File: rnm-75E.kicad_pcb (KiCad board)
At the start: 2 copper layers, 323.8 x 114.3 mm, 217 parts, among them J1 AVR-ISP-6, J2 USB_C_Receptacle_USB2.0, J3 Conn_01x04, SW1 SW_Push, SW2 Rotary_Encoder_Switch, U1 AT90USB646-AU, Y1 Crystal_GND24_Small

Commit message: WIRED SPI
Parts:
- C_ucap1, SW1: moved to B.Cu
- moved J1 311.5 mm to (646.9, -4.76)
- moved C_ucap1 168.3 mm to (523.1, 64.3), turned to 180 degrees
- moved SW1 125.0 mm to (585.7, 67.7), turned to 0 degrees
- moved R1 6.74 mm to (648.5, -20.8)
- moved CF3 6.70 mm to (530.4, 69.1), turned to 0 degrees
- moved D57 5.02 mm to (537.4, 55.6), turned to 270 degrees
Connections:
- U1 pad 10: LED_PIN -> LED
- U1 pad 9: LED -> LED_PIN
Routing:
- net LED_PIN: track 31.0 -> 263.2 mm, vias 0 -> 1
- net MOSI: track 0.00 -> 204.9 mm
- net GND: track 36.3 -> 237.6 mm
- net MISO: track 0.00 -> 185.3 mm, vias 0 -> 2
- net SCK: track 0.00 -> 183.9 mm
- net RESET: track 0.00 -> 70.9 mm
- net Net-(C_ucap1-Pad2): track 0.00 -> 17.4 mm
- net +5V: track 233.0 -> 249.0 mm, vias 0 -> 2
- net Net-(CAPS_LOCK_LED1-Pad1): track 23.6 -> 28.4 mm
- net Net-(D57-Pad2): track 6.82 -> 4.62 mm
- net ROWE: track 0.00 -> 0.67 mm

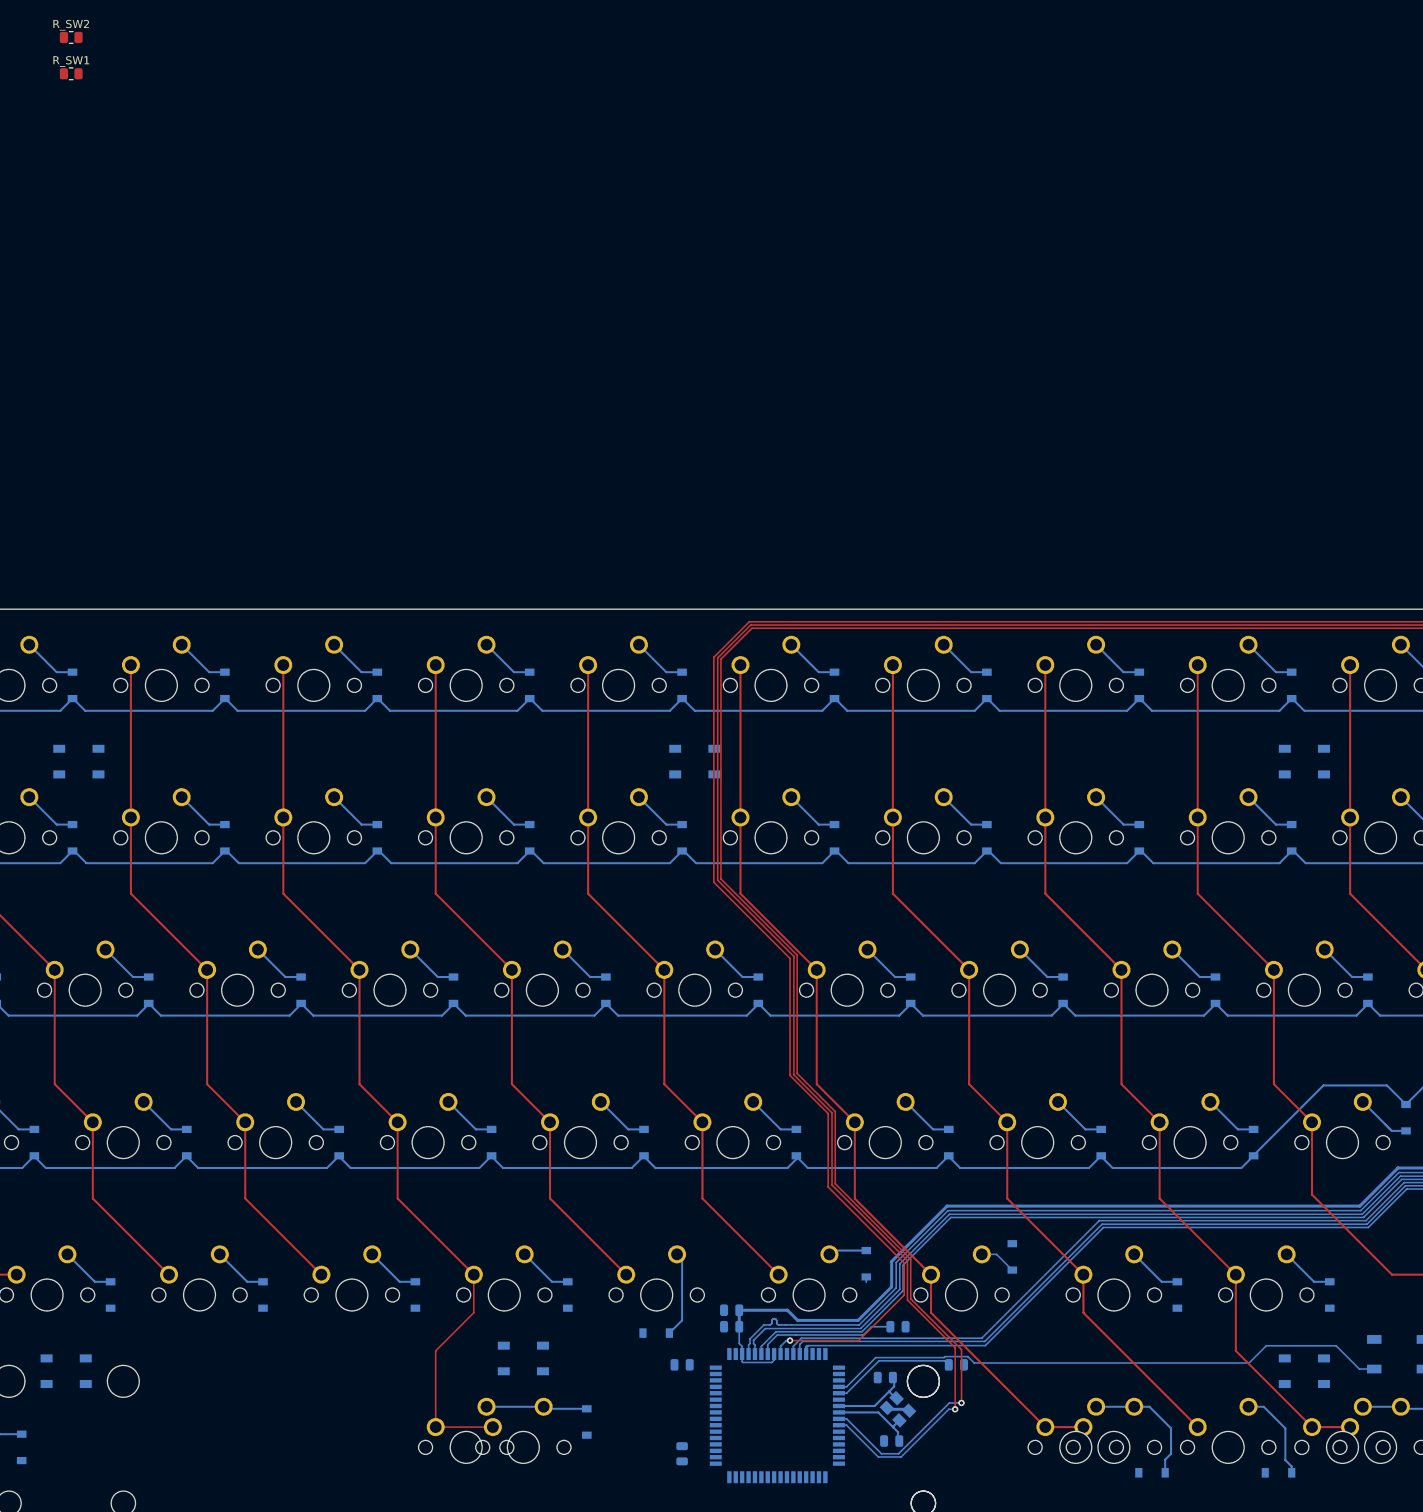
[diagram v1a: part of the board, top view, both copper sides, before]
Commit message: move sw res
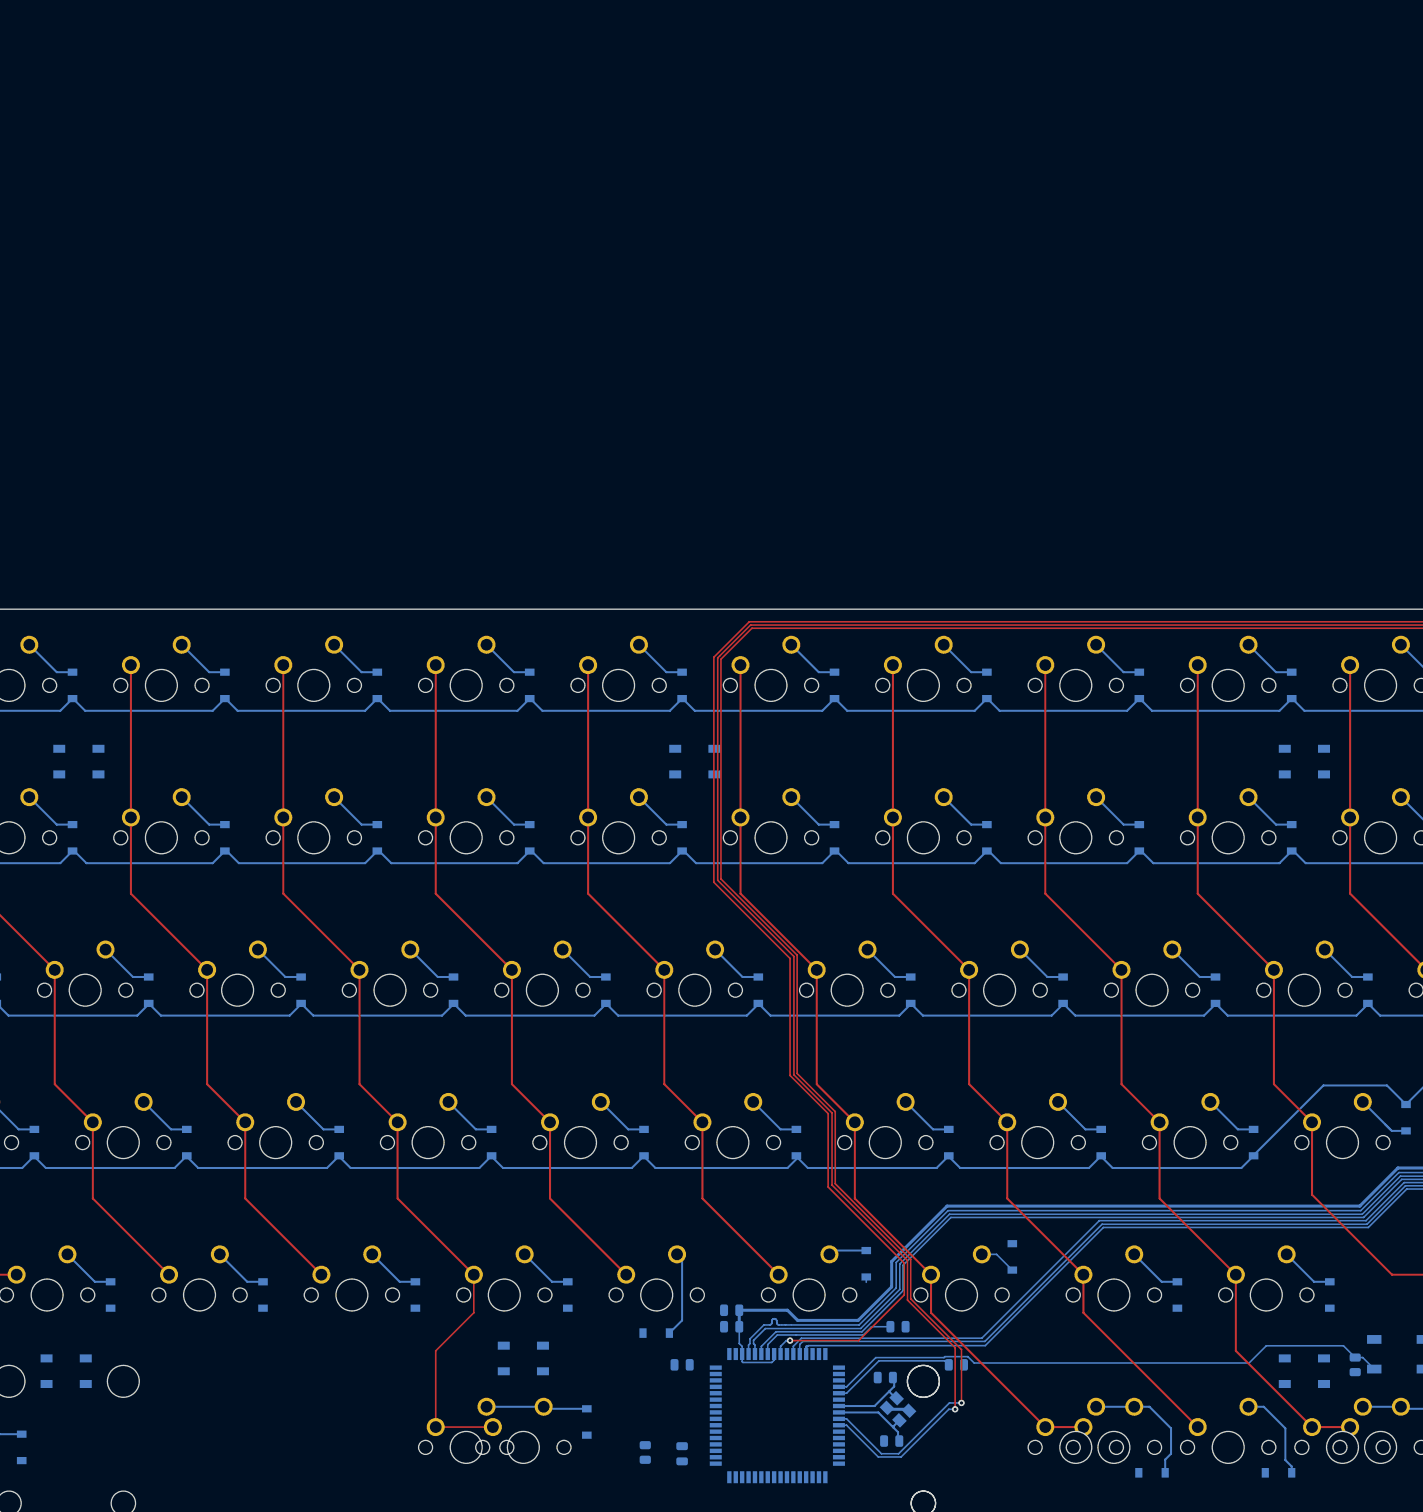
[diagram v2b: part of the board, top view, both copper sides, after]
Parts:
- R_SW1, R_SW2: moved to B.Cu
- moved R_SW1 227.6 mm to (580.2, 69.1), turned to 270 degrees
- moved R_SW2 190.9 mm to (491.5, 80.0), turned to 90 degrees

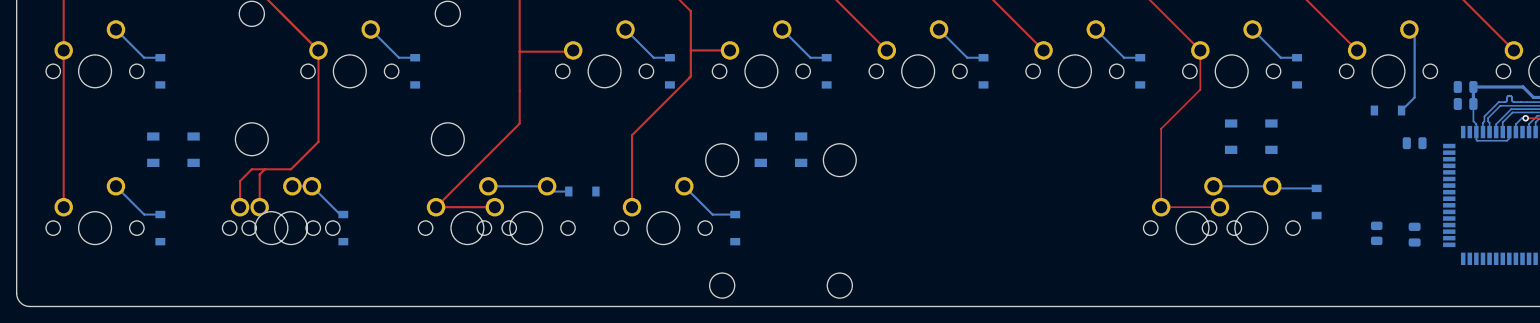
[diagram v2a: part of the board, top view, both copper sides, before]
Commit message: route column 1-6
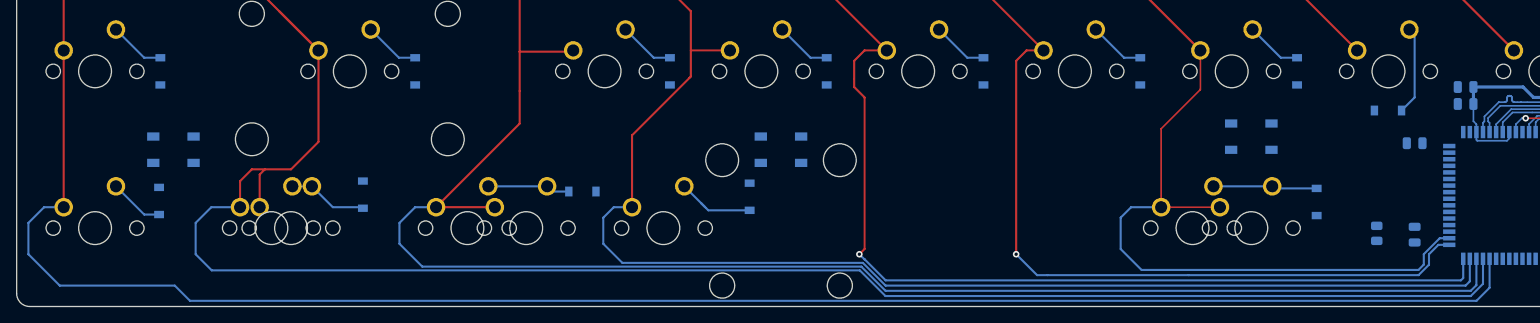
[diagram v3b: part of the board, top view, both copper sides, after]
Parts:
- moved D11 4.71 mm to (368.3, 75.3), turned to 270 degrees
- moved D20 4.19 mm to (415.3, 75.6), turned to 270 degrees
- moved D5 3.30 mm to (343.5, 76.1), turned to 270 degrees
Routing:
- net COL0: track 103.8 -> 296.8 mm
- net COL1: track 125.3 -> 297.4 mm
- net COL2: track 120.3 -> 264.8 mm
- net COL3: track 110.9 -> 228.4 mm
- net COL4: track 86.1 -> 192.1 mm, vias 0 -> 1
- net COL5: track 86.1 -> 169.4 mm, vias 0 -> 1
- net COL6: track 114.2 -> 166.8 mm
- net Net-(D20-Pad2): track 7.61 -> 9.82 mm
- net Net-(D11-Pad2): track 7.61 -> 9.68 mm

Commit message: route c7/8
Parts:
- moved C_F2 5.74 mm to (494.7, 74.6)
- moved R_SW2 5.47 mm to (490.9, 74.6)
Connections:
- U1 pad 17: (no net) -> COL8
- U1 pad 54: COL8 -> (no net)
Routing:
- net COL7: track 86.1 -> 129.9 mm, vias 0 -> 1
- net COL8: track 86.1 -> 114.6 mm, vias 0 -> 1

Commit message: row 7 connected
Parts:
- moved D46 12.4 mm to (499.1, 54.4), turned to 270 degrees
- moved C_F2 7.95 mm to (495.0, 82.5), turned to 180 degrees
- moved D87 4.89 mm to (647.7, 36.5), turned to 270 degrees
- moved D69 3.33 mm to (576.6, 57.0), turned to 270 degrees
- moved D75 3.31 mm to (603.0, 53.9), turned to 270 degrees
- moved D81 3.30 mm to (629.4, 57.0), turned to 270 degrees
- moved D63 3.30 mm to (558.0, 57.0), turned to 270 degrees
- moved D88 3.30 mm to (648.5, 57.0), turned to 270 degrees
- moved D51 2.09 mm to (518.8, 54.4), turned to 270 degrees
- moved C_X1 1.94 mm to (520.7, 77.5), turned to 135 degrees
- moved D41 1.72 mm to (483.4, 74.7), turned to 270 degrees
- moved C_X2 1.37 mm to (520.7, 71.8), turned to 225 degrees
- moved C_F4 1.21 mm to (497.2, 68.6), turned to 90 degrees
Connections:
- U1 pad 18: (no net) -> COL9
- U1 pad 19: (no net) -> COL10
- U1 pad 27: ROWF -> (no net)
- U1 pad 54: (no net) -> COL15
- U1 pad 55: COL9 -> (no net)
- U1 pad 56: COL10 -> (no net)
- U1 pad 61: COL15 -> ROWF
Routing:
- net ROWF: track 0.00 -> 373.4 mm, vias 0 -> 2
- net ROWE: track 0.67 -> 327.9 mm, vias 0 -> 4
- net +5V: track 249.0 -> 345.4 mm, vias 2 -> 6
- net COL10: track 111.0 -> 173.7 mm, vias 0 -> 1
- net ROWC: track 283.5 -> 324.9 mm, vias 0 -> 2
- net ROWD: track 293.7 -> 328.9 mm, vias 0 -> 2
- net ROWB: track 294.0 -> 324.5 mm, vias 0 -> 2
- net COL9: track 115.8 -> 145.7 mm, vias 0 -> 1
- net GND: track 237.6 -> 255.6 mm
- net Net-(D46-Pad2): track 10.8 -> 4.86 mm
- net COL8: track 114.6 -> 109.9 mm
- net Net-(D87-Pad2): track 6.82 -> 5.39 mm

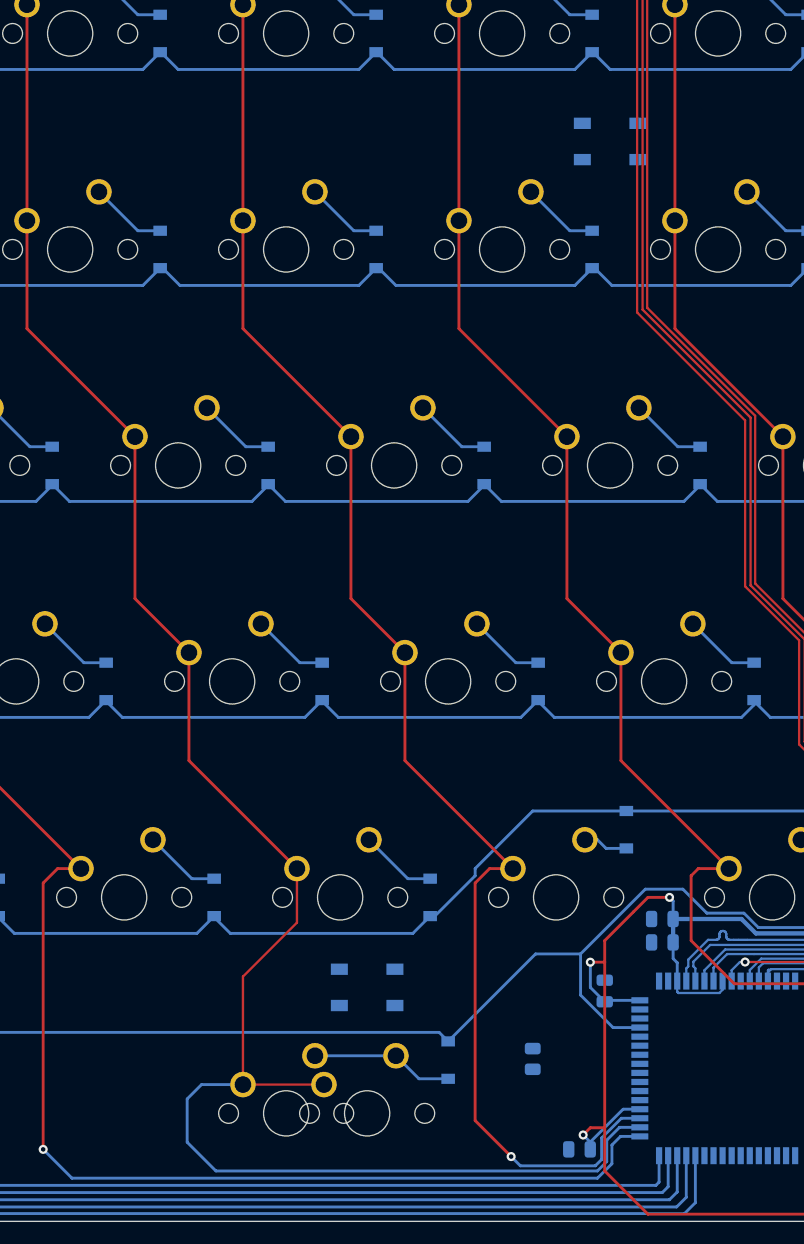
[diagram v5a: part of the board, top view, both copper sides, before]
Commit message: route row A-E onto mcu
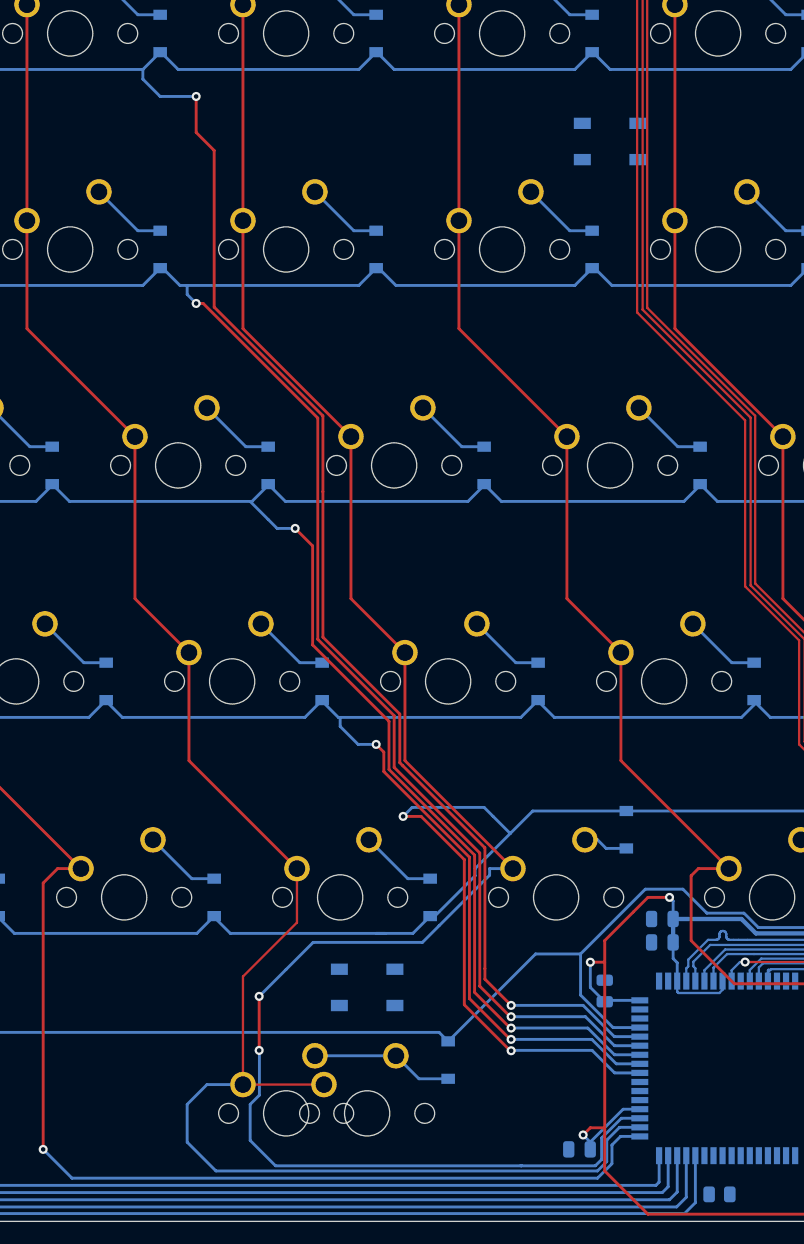
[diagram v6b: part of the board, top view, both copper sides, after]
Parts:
- moved R_SW2 20.3 mm to (507.3, 86.5), turned to 0 degrees
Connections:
- U1 pad 28: ROWE -> COL15
- U1 pad 29: ROWD -> COL14
- U1 pad 30: ROWC -> COL13
- U1 pad 31: ROWB -> COL12
- U1 pad 32: ROWA -> COL11
- U1 pad 54: COL15 -> (no net)
- U1 pad 56: (no net) -> ROWE
- U1 pad 57: COL11 -> ROWD
- U1 pad 58: COL12 -> ROWC
- U1 pad 59: COL13 -> ROWB
- U1 pad 60: COL14 -> ROWA
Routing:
- net ROWA: track 280.6 -> 390.9 mm, vias 0 -> 2
- net ROWB: track 324.5 -> 413.6 mm, vias 2 -> 4
- net ROWC: track 324.9 -> 394.1 mm, vias 2 -> 4
- net ROWE: track 327.9 -> 377.2 mm, vias 4 -> 6
- net ROWD: track 328.9 -> 376.8 mm, vias 2 -> 4
- net COL7: track 129.9 -> 164.8 mm, vias 1 -> 2
